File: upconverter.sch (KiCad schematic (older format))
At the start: 35 parts, among them J1 Barrel_Jack, J2 SMA_F, J3 SMA_F, U1 L7805, U2 TPS71533__SC70, U3 SA602A, X1 XO32

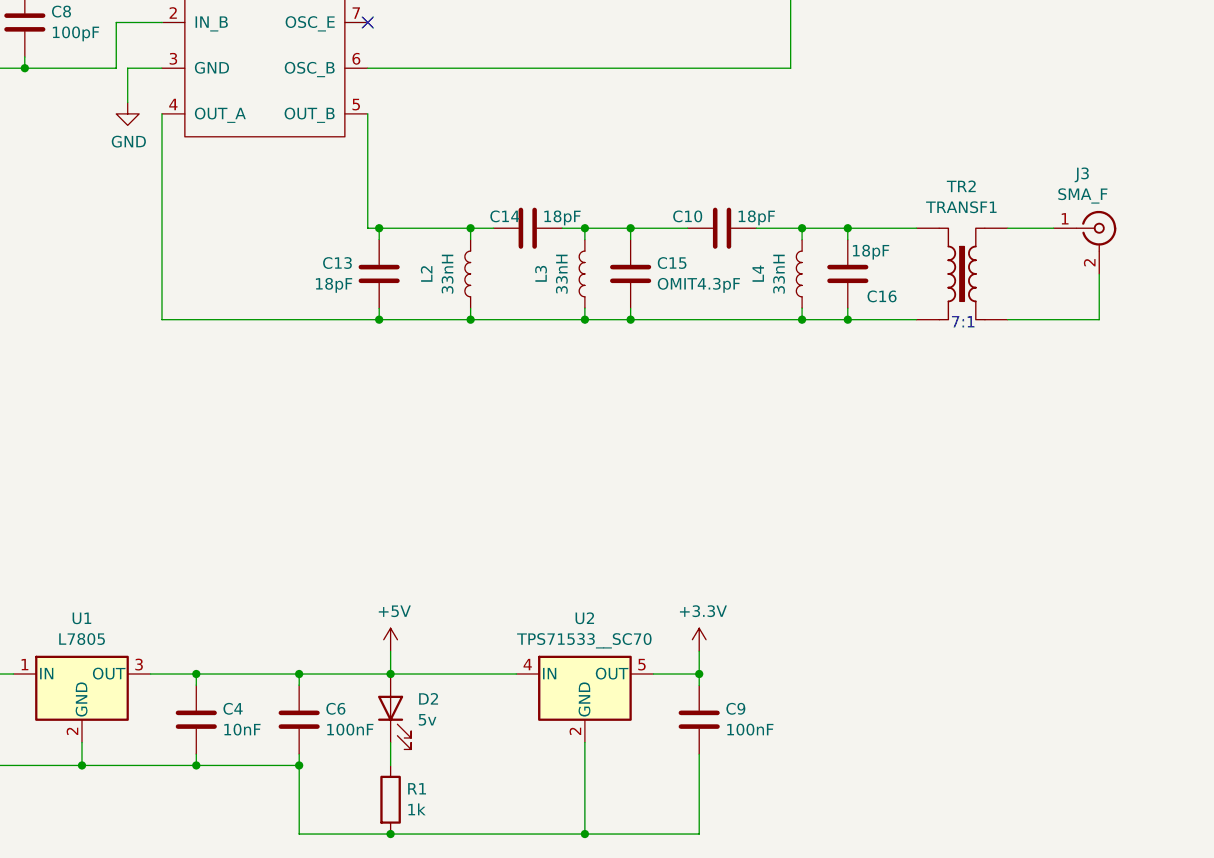
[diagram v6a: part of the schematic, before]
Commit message: Board edge, tracks. Need to finish DRC fixes & JLCPCB setup
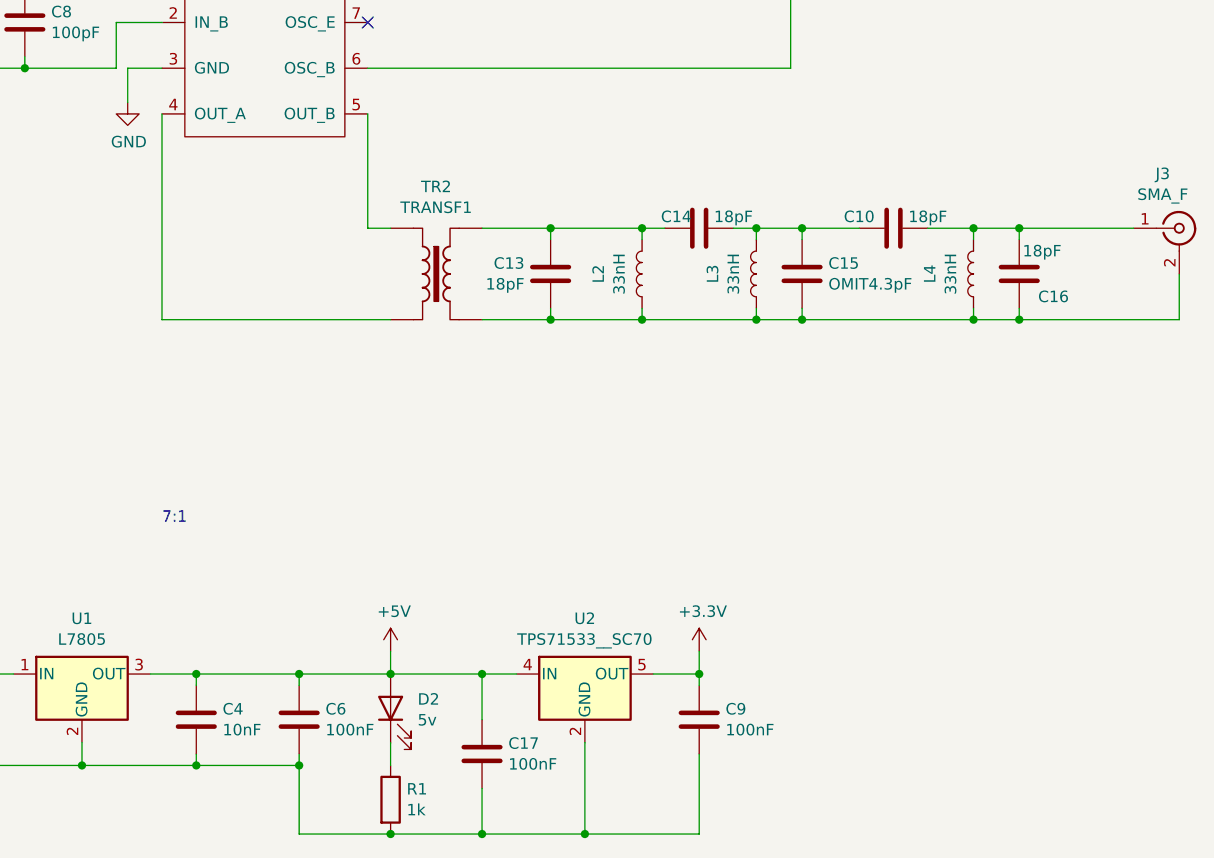
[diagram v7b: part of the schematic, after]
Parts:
- added C17: 100nF, Capacitor_SMD:C_0805_2012Metric, symbol Device:C
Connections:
- net +5V: now also C17.1
- net GND: now also C17.2
- net at C13.1, C15.2, C16.1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: now also J3.2 (Ext), TR2.3; no longer TR2.2, U3.4 (OUT_A)
- net at C13.2, C14.2, L2.2: now also TR2.4; no longer U3.5 (OUT_B)
- net at J3.1 (In): now also C10.2, C16.2, L4.2; no longer TR2.4
- new net: TR2.2, U3.4 (OUT_A)
- new net: TR2.1, U3.5 (OUT_B)
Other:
- moved on the sheet: C10, C13, C14, C15, C16, J3, L2, L3, L4, TR2
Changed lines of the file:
@@
 L Connector:Conn_Coaxial J3
 U 1 1 5EFAC751
-P 12050 4950
-F 0 "J3" H 11978 5188 50  0000 C CNN
-F 1 "SMA_F" H 11978 5097 50  0000 C CNN
-F 2 "Connector_Coaxial:SMA_Amphenol_901-144_Vertical" H 12050 4950 50  0001 C CNN
-F 3 " ~" H 12050 4950 50  0001 C CNN
-	1    12050 4950
+P 12400 4950
+F 0 "J3" H 12328 5188 50  0000 C CNN
+F 1 "SMA_F" H 12328 5097 50  0000 C CNN
+F 2 "Connector_Coaxial:SMA_Amphenol_901-144_Vertical" H 12400 4950 50  0001 C CNN
+F 3 " ~" H 12400 4950 50  0001 C CNN
+	1    12400 4950
 	1    0    0    -1
 $EndComp
@@
 L Transformer:TRANSF1 TR2
 U 1 1 60F90E80
-P 11450 5150
-F 0 "TR2" H 11450 5531 50  0000 C CNN
-F 1 "TRANSF1" H 11450 5440 50  0000 C CNN
-F 2 "ZAM_Custom:fair-rite_2643625002" H 11450 5150 50  0001 C CNN
-F 3 "" H 11450 5150 50  0001 C CNN
-	1    11450 5150
+P 9150 5150
+F 0 "TR2" H 9150 5531 50  0000 C CNN
+F 1 "TRANSF1" H 9150 5440 50  0000 C CNN
+F 2 "ZAM_Custom:fair-rite_2643625002" H 9150 5150 50  0001 C CNN
+F 3 "" H 9150 5150 50  0001 C CNN
+	1    9150 5150
 	1    0    0    -1
 $EndComp
@@
 L Device:C C10
 U 1 1 60F9E5B1
-P 10400 4950
-F 0 "C10" V 10450 5100 50  0000 C CNN
-F 1 "18pF" V 10450 4800 50  0000 C CNN
-F 2 "Capacitor_SMD:C_0805_2012Metric" H 10438 4800 50  0001 C CNN
-F 3 "~" H 10400 4950 50  0001 C CNN
-	1    10400 4950
+P 11150 4950
+F 0 "C10" V 11200 5100 50  0000 C CNN
+F 1 "18pF" V 11200 4800 50  0000 C CNN
+F 2 "Capacitor_SMD:C_0805_2012Metric" H 11188 4800 50  0001 C CNN
+F 3 "~" H 11150 4950 50  0001 C CNN
+	1    11150 4950
 	0    -1   -1   0
 $EndComp
-Wire Wire Line
-	10950 4950 11250 4950
-Wire Wire Line
-	11650 4950 11850 4950
 Wire Wire Line
 	5950 6900 6350 6900
@@
 $EndComp
 Wire Wire Line
-	9500 6900 8950 6900
+	9500 6900 9350 6900
 Connection ~ 8950 6900
 Wire Wire Line
 	9800 7200 9800 7600
-Wire Wire Line
-	9800 7600 8950 7600
 Connection ~ 8950 7600
 $Comp
@@
 Wire Wire Line
 	7800 4250 7800 4400
-Text Notes 11400 5400 0    50   ~ 0
+Text Notes 7950 6250 0    50   ~ 0
 7:1
 Text Notes 5450 4500 0    50   ~ 0
 TODO: preamp?
 Wire Wire Line
-	12050 5150 12050 5350
-Wire Wire Line
-	12050 5350 11650 5350
-Wire Wire Line
-	10950 5350 10950 5300
-Wire Wire Line
-	10950 5350 11250 5350
-Connection ~ 10950 5350
-Wire Wire Line
-	10950 5000 10950 4950
+	12400 5150 12400 5350
+Wire Wire Line
+	11700 5350 11700 5300
+Connection ~ 11700 5350
+Wire Wire Line
+	11700 5000 11700 4950
 $Comp
 L Device:L L4
 U 1 1 60F8630A
+P 11500 5150
+F 0 "L4" V 11690 5150 50  0000 C CNN
+F 1 "33nH" V 11599 5150 50  0000 C CNN
+F 2 "Inductor_SMD:L_0805_2012Metric" H 11500 5150 50  0001 C CNN
+F 3 "~" H 11500 5150 50  0001 C CNN
+	1    11500 5150
+	-1   0    0    1
+$EndComp
+$Comp
+L Device:C C15
+U 1 1 60F8754D
 P 10750 5150
-F 0 "L4" V 10940 5150 50  0000 C CNN
-F 1 "33nH" V 10849 5150 50  0000 C CNN
-F 2 "Inductor_SMD:L_0805_2012Metric" H 10750 5150 50  0001 C CNN
+F 0 "C15" H 10865 5196 50  0000 L CNN
+F 1 "OMIT4.3pF" H 10865 5105 50  0000 L CNN
+F 2 "Capacitor_SMD:C_0603_1608Metric" H 10788 5000 50  0001 C CNN
 F 3 "~" H 10750 5150 50  0001 C CNN
 	1    10750 5150
-	-1   0    0    1
-$EndComp
-$Comp
-L Device:C C15
-U 1 1 60F8754D
-P 10000 5150
-F 0 "C15" H 10115 5196 50  0000 L CNN
-F 1 "OMIT4.3pF" H 10115 5105 50  0000 L CNN
-F 2 "Capacitor_SMD:C_0603_1608Metric" H 10038 5000 50  0001 C CNN
-F 3 "~" H 10000 5150 50  0001 C CNN
-	1    10000 5150
-	1    0    0    -1
-$EndComp
-Wire Wire Line
-	10000 4950 10000 5000
-Wire Wire Line
-	10000 5300 10000 5350
-Connection ~ 10000 5350
-Wire Wire Line
-	10000 5350 10750 5350
-Wire Wire Line
-	10000 4950 9800 4950
-Connection ~ 10000 4950
+	1    0    0    -1
+$EndComp
+Wire Wire Line
+	10750 4950 10750 5000
+Wire Wire Line
+	10750 5300 10750 5350
+Connection ~ 10750 5350
+Wire Wire Line
+	10750 5350 11500 5350
+Wire Wire Line
+	10750 4950 10550 4950
+Connection ~ 10750 4950
 $Comp
 L Device:C C14
 U 1 1 60F97BD9
-P 9550 4950
-F 0 "C14" V 9500 4850 50  0000 C CNN
-F 1 "18pF" V 9500 5100 50  0000 C CNN
-F 2 "Capacitor_SMD:C_0603_1608Metric" H 9588 4800 50  0001 C CNN
-F 3 "~" H 9550 4950 50  0001 C CNN
-	1    9550 4950
+P 10300 4950
+F 0 "C14" V 10250 4850 50  0000 C CNN
+F 1 "18pF" V 10250 5100 50  0000 C CNN
+F 2 "Capacitor_SMD:C_0603_1608Metric" H 10338 4800 50  0001 C CNN
+F 3 "~" H 10300 4950 50  0001 C CNN
+	1    10300 4950
 	0    1    1    0
 $EndComp
@@
 L Device:L L2
 U 1 1 60F9F8BE
-P 9300 5150
-F 0 "L2" V 9490 5150 50  0000 C CNN
-F 1 "33nH" V 9399 5150 50  0000 C CNN
-F 2 "Inductor_SMD:L_0805_2012Metric" H 9300 5150 50  0001 C CNN
-F 3 "~" H 9300 5150 50  0001 C CNN
-	1    9300 5150
+P 10050 5150
+F 0 "L2" V 10240 5150 50  0000 C CNN
+F 1 "33nH" V 10149 5150 50  0000 C CNN
+F 2 "Inductor_SMD:L_0805_2012Metric" H 10050 5150 50  0001 C CNN
+F 3 "~" H 10050 5150 50  0001 C CNN
+	1    10050 5150
 	-1   0    0    1
 $EndComp
 Wire Wire Line
-	9400 4950 9300 4950
-Wire Wire Line
-	9300 4950 9300 5000
-Wire Wire Line
-	9300 5300 9300 5350
-Connection ~ 9300 5350
-Wire Wire Line
-	9300 5350 9800 5350
+	10150 4950 10050 4950
+Wire Wire Line
+	10050 4950 10050 5000
+Wire Wire Line
+	10050 5300 10050 5350
+Connection ~ 10050 5350
+Wire Wire Line
+	10050 5350 10550 5350
 $Comp
 L Device:C C13
 U 1 1 60FA5B8C
-P 8900 5150
-F 0 "C13" H 8786 5104 50  0000 R CNN
-F 1 "18pF" H 8786 5195 50  0000 R CNN
-F 2 "Capacitor_SMD:C_0603_1608Metric" H 8938 5000 50  0001 C CNN
-F 3 "~" H 8900 5150 50  0001 C CNN
-	1    8900 5150
+P 9650 5150
+F 0 "C13" H 9536 5104 50  0000 R CNN
+F 1 "18pF" H 9536 5195 50  0000 R CNN
+F 2 "Capacitor_SMD:C_0603_1608Metric" H 9688 5000 50  0001 C CNN
+F 3 "~" H 9650 5150 50  0001 C CNN
+	1    9650 5150
 	1    0    0    1
 $EndComp
-Connection ~ 9300 4950
+Connection ~ 10050 4950
 Wire Wire Line
 	8850 4450 8850 4950
-Wire Wire Line
-	7950 5350 8900 5350
 Wire Wire Line
 	7950 4450 7950 5350
@@
 L Device:L L3
 U 1 1 60FAE8DB
-P 9800 5150
-F 0 "L3" V 9990 5150 50  0000 C CNN
-F 1 "33nH" V 9899 5150 50  0000 C CNN
-F 2 "Inductor_SMD:L_0805_2012Metric" H 9800 5150 50  0001 C CNN
-F 3 "~" H 9800 5150 50  0001 C CNN
-	1    9800 5150
+P 10550 5150
+F 0 "L3" V 10740 5150 50  0000 C CNN
+F 1 "33nH" V 10649 5150 50  0000 C CNN
+F 2 "Inductor_SMD:L_0805_2012Metric" H 10550 5150 50  0001 C CNN
+F 3 "~" H 10550 5150 50  0001 C CNN
+	1    10550 5150
 	-1   0    0    1
 $EndComp
 Wire Wire Line
-	8900 5000 8900 4950
-Connection ~ 8900 4950
-Wire Wire Line
-	8900 4950 8850 4950
-Wire Wire Line
-	8900 4950 9300 4950
-Wire Wire Line
-	8900 5300 8900 5350
-Connection ~ 8900 5350
-Wire Wire Line
-	8900 5350 9300 5350
-Wire Wire Line
-	9800 5000 9800 4950
-Connection ~ 9800 4950
-Wire Wire Line
-	9800 4950 9700 4950
-Wire Wire Line
-	9800 5300 9800 5350
-Connection ~ 9800 5350
-Wire Wire Line
-	9800 5350 10000 5350
-Wire Wire Line
-	10000 4950 10250 4950
-Wire Wire Line
-	10550 4950 10750 4950
-Wire Wire Line
-	10750 4950 10750 5000
-Wire Wire Line
-	10750 5300 10750 5350
-Connection ~ 10750 5350
-Wire Wire Line
-	10750 5350 10950 5350
+	9650 5000 9650 4950
+Connection ~ 9650 4950
+Wire Wire Line
+	9650 4950 10050 4950
+Wire Wire Line
+	9650 5300 9650 5350
+Wire Wire Line
+	9650 5350 10050 5350
+Wire Wire Line
+	10550 5000 10550 4950
+Connection ~ 10550 4950
+Wire Wire Line
+	10550 4950 10450 4950
+Wire Wire Line
+	10550 5300 10550 5350
+Connection ~ 10550 5350
+Wire Wire Line
+	10550 5350 10750 5350
+Wire Wire Line
+	10750 4950 11000 4950
+Wire Wire Line
+	11300 4950 11500 4950
+Wire Wire Line
+	11500 4950 11500 5000
+Wire Wire Line
+	11500 5300 11500 5350
+Connection ~ 11500 5350
+Wire Wire Line
+	11500 5350 11700 5350
 $Comp
 L Device:C C16
 U 1 1 60FD7697
-P 10950 5150
-F 0 "C16" H 10800 5250 50  0000 C CNN
-F 1 "18pF" H 10850 5050 50  0000 C CNN
-F 2 "Capacitor_SMD:C_0805_2012Metric" H 10988 5000 50  0001 C CNN
-F 3 "~" H 10950 5150 50  0001 C CNN
-	1    10950 5150
+P 11700 5150
+F 0 "C16" H 11550 5250 50  0000 C CNN
+F 1 "18pF" H 11600 5050 50  0000 C CNN
+F 2 "Capacitor_SMD:C_0805_2012Metric" H 11738 5000 50  0001 C CNN
+F 3 "~" H 11700 5150 50  0001 C CNN
+	1    11700 5150
 	-1   0    0    1
 $EndComp
 Wire Wire Line
-	10950 4950 10750 4950
-Connection ~ 10950 4950
-Connection ~ 10750 4950
+	11700 4950 11500 4950
+Connection ~ 11700 4950
+Connection ~ 11500 4950
 Text Notes 6850 4350 0    50   ~ 0
 1:7
@@
 	1    0    0    -1
 $EndComp
+Wire Wire Line
+	11700 4950 12200 4950
+Wire Wire Line
+	11700 5350 12400 5350
+Wire Wire Line
+	8950 4950 8850 4950
+Wire Wire Line
+	8950 5350 7950 5350
+Wire Wire Line
+	9350 4950 9650 4950
+Wire Wire Line
+	9350 5350 9650 5350
+Connection ~ 9650 5350
+$Comp
+L Device:C C17
+U 1 1 60FEB847
+P 9350 7250
+F 0 "C17" H 9465 7296 50  0000 L CNN
+F 1 "100nF" H 9465 7205 50  0000 L CNN
+F 2 "Capacitor_SMD:C_0805_2012Metric" H 9388 7100 50  0001 C CNN
+F 3 "~" H 9350 7250 50  0001 C CNN
+	1    9350 7250
+	1    0    0    -1
+$EndComp
+Wire Wire Line
+	9350 7100 9350 6900
+Connection ~ 9350 6900
+Wire Wire Line
+	9350 6900 8950 6900
+Wire Wire Line
+	9350 7400 9350 7600
+Wire Wire Line
+	8950 7600 9350 7600
+Connection ~ 9350 7600
+Wire Wire Line
+	9350 7600 9800 7600
 $EndSCHEMATC

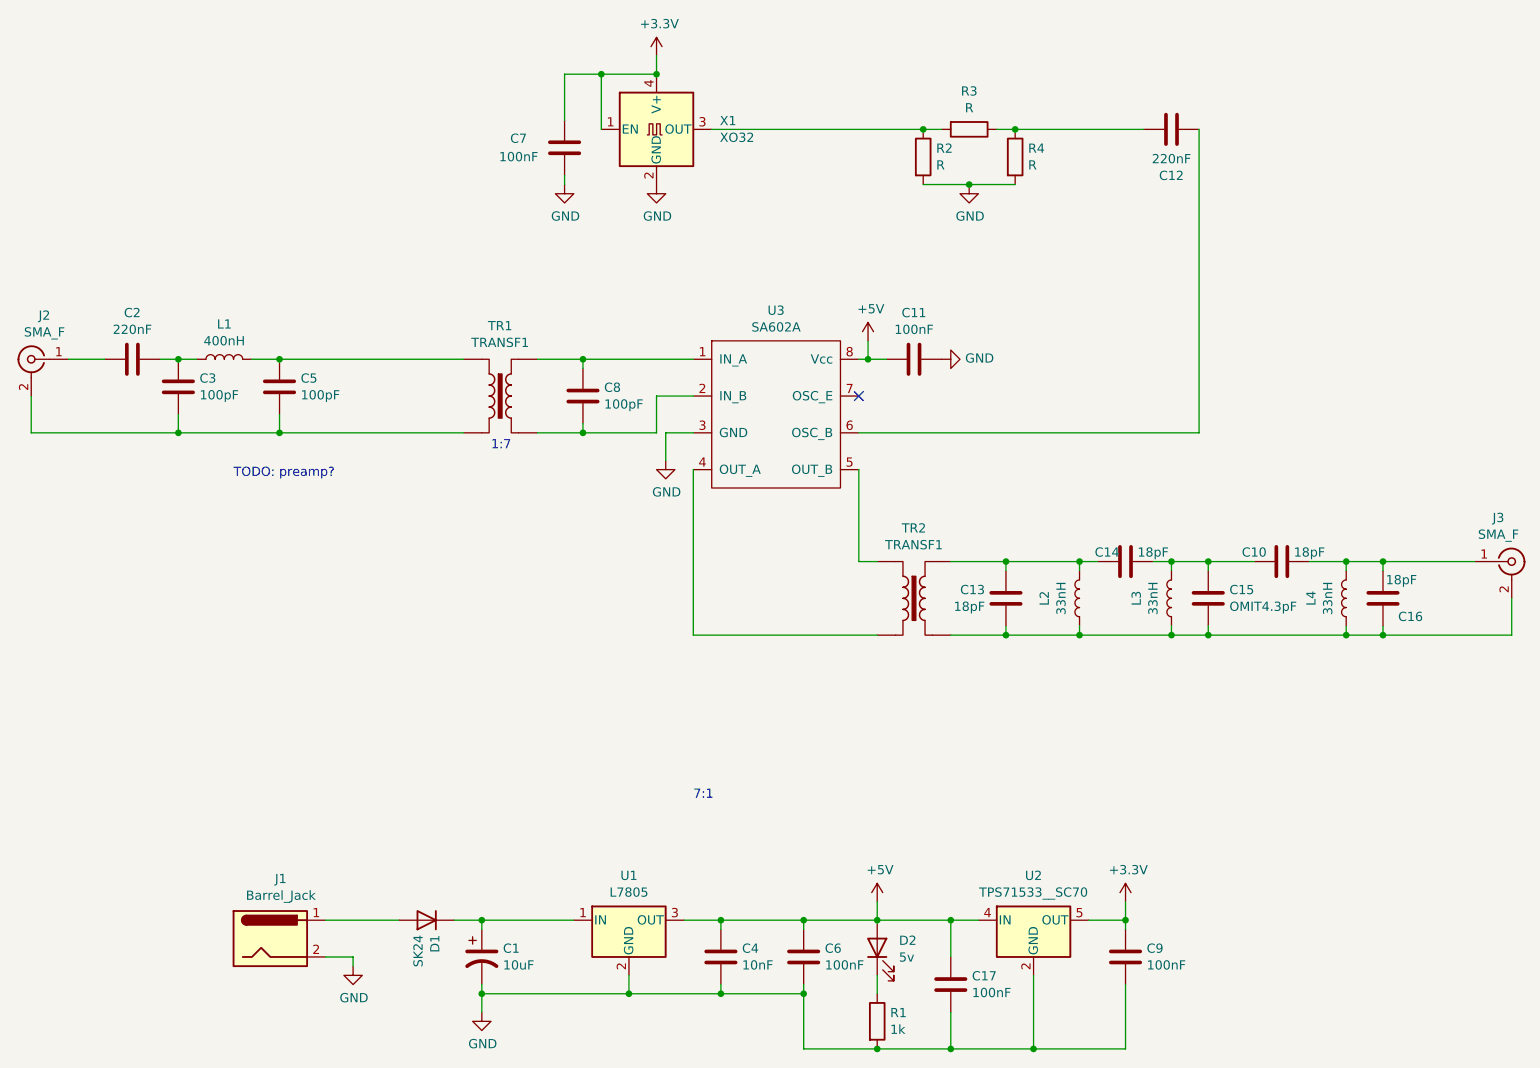
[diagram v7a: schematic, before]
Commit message: Updated schematic for experimental single-ended input/output. TODO: test if it works, test i/o characteristics. Note impedance issue vs balun
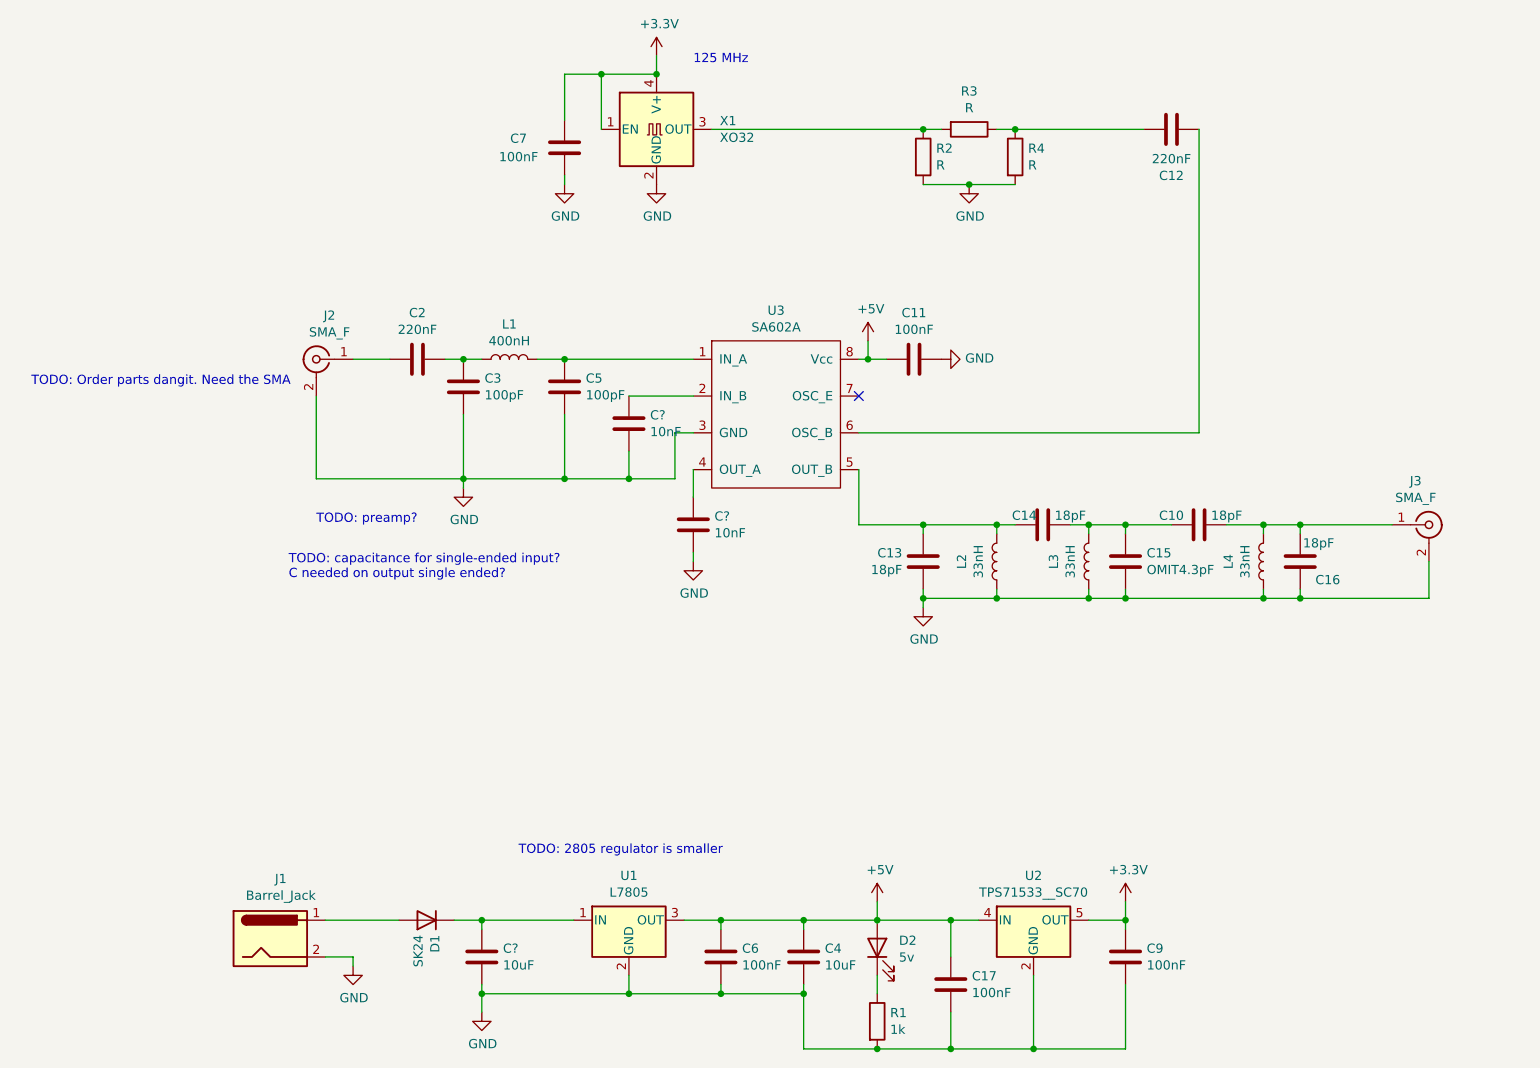
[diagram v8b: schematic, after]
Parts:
- removed C1: 10uF, Capacitor_SMD:C_0805_2012Metric, symbol Device:CP1
- removed C8: 100pF, Capacitor_SMD:C_0603_1608Metric, symbol Device:C
- removed TR1, TR2: TRANSF1, ZAM_Custom:fair-rite_2643625002, symbol Transformer:TRANSF1
- added C? (x2): 10nF, Capacitor_SMD:C_0603_1608Metric, symbol Device:C
- added C?: 10uF, Capacitor_SMD:C_0805_2012Metric, symbol Device:C
- C4: value 10nF -> 10uF
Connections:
- net GND: now also C13.1, C15.2, C16.1, C3.2, C5.2, J2.2 (Ext), J3.2 (Ext), L2.1, L3.1, L4.1, C?.2, C?.2, C?.2
- net at U3.1 (IN_A): now also C5.1, L1.2
- net at U3.2 (IN_B): now also C?.1
- net at U3.4 (OUT_A): now also C?.1
- net at U3.5 (OUT_B): now also C13.2, C14.2, L2.2
- net at D1.1 (K), U1.1 (IN): now also C?.1
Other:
- note added: "125 MHz"
- note added: "TODO: 2805 regulator is smaller"
- note added: "TODO: Order parts dangit. Need the SMA\n"
- note added: "TODO: capacitance for single-ended input?\nC needed on output single ended?"
- note removed: "1:7"
- note removed: "7:1"
- moved on the sheet: C10, C13, C14, C15, C16, C2, C3, C4, C5, C6, J2, J3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
